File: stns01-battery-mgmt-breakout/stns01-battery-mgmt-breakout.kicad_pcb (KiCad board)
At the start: 2 copper layers, 0 parts

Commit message: Generate BOM. Initial parts placement.
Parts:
- added C1: 2.2uF, Wickerlib:RLC-0603-SMD, F.Cu at (62.5, 44.0)
- added C2: 4.7uF, Wickerlib:RLC-0603-SMD, F.Cu at (64.2, 55.1)
- added C3: 2.2uF, Wickerlib:RLC-0603-SMD, F.Cu at (72.6, 55.8)
- added C4: 2.2uF, Wickerlib:RLC-0603-SMD, F.Cu at (70.4, 55.8)
- added J1: MICRO USB, Wickerlib:CONN-USB-MICRO-B-AMPHENOL-10118193-0001LF, F.Cu at (56.5, 44.0)
- added J2: PH, Wickerlib:CONN-JST-S2B-PH-SM4-TB, F.Cu at (55.7, 55.1)
- added J3: POWER PINS, Wickerlib:CONN-HEADER-STRAIGHT-P2.54MM-1x07, F.Cu at (91.9, 47.4)
- added J4: CONTROL PINS, Wickerlib:CONN-HEADER-STRAIGHT-P2.54MM-1x07, F.Cu at (72.8, 74.7)
- added LED1: RED, Wickerlib:LED-0603-SMD, F.Cu at (76.5, 58.0)
- added R1: 0 ohm, Wickerlib:RLC-0603-SMD, F.Cu at (80.7, 53.6)
- added R2: 10K, Wickerlib:RLC-0603-SMD, F.Cu at (80.9, 56.1)
- added R3: NTC 10K, Wickerlib:RLC-0603-SMD, F.Cu at (80.8, 58.0)
- added R4: 604, Wickerlib:RLC-0603-SMD, F.Cu at (76.6, 61.1)
- added R5: 10K, Wickerlib:RLC-0603-SMD, F.Cu at (80.8, 54.5)
- added R6: 10K, Wickerlib:RLC-0603-SMD, F.Cu at (85.8, 55.4)
- added S1: SHUNT, Wickerlib:CONN-HEADER-STRAIGHT-P2.54MM-1x03, F.Cu at (82.2, 40.3)
- added S2: SLIDE, Wickerlib:SWITCH-ESWITCH-SLIDE-TH-EG1218, F.Cu at (100.1, 39.5)
- added U1: STNS01, Wickerlib:DFN-12-1EP-3x3MM-P0.45MM, F.Cu at (76.5, 54.5)
- added U2: LDO REG 3.3V, Wickerlib:SOT-23-3, F.Cu at (76.9, 48.1)
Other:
- rule trace_clearance: 0.1524 -> 0.254

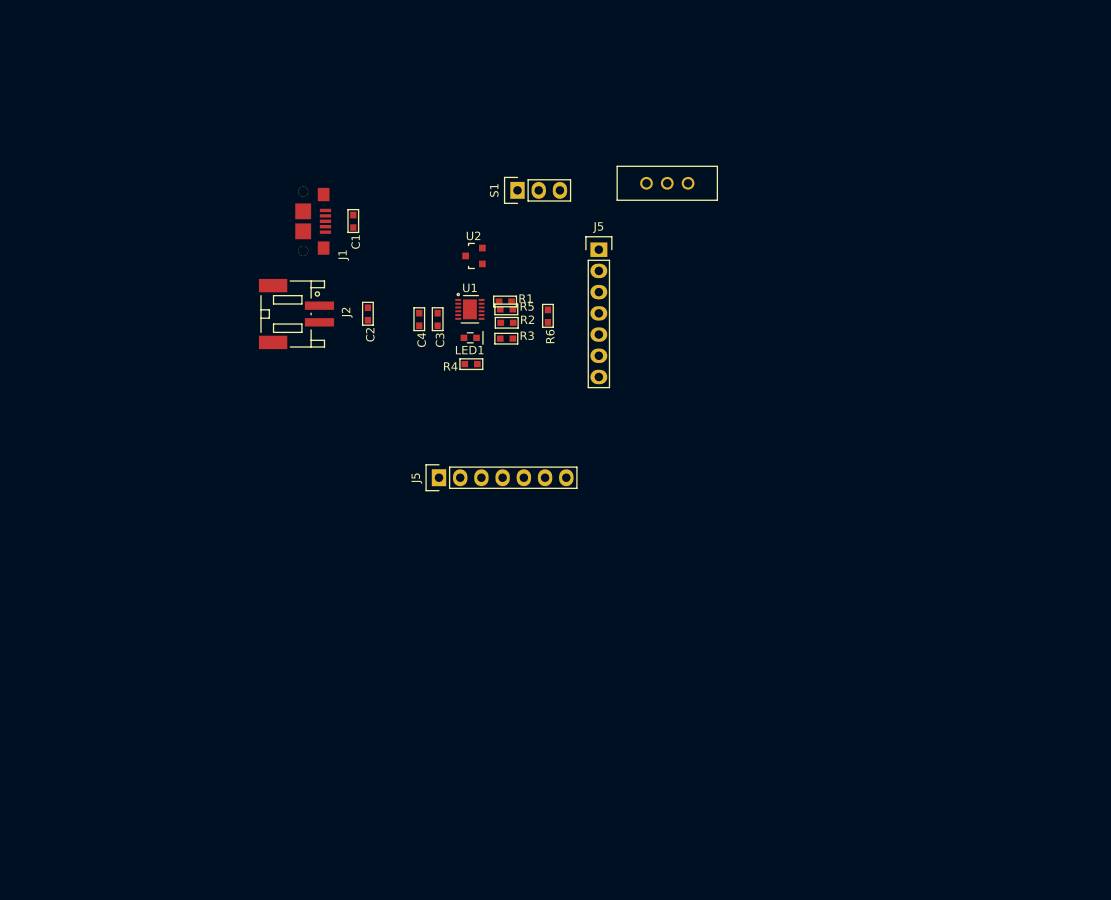
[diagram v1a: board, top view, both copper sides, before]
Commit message: Release v1.0 STNS01 battery breakout, needs tested.
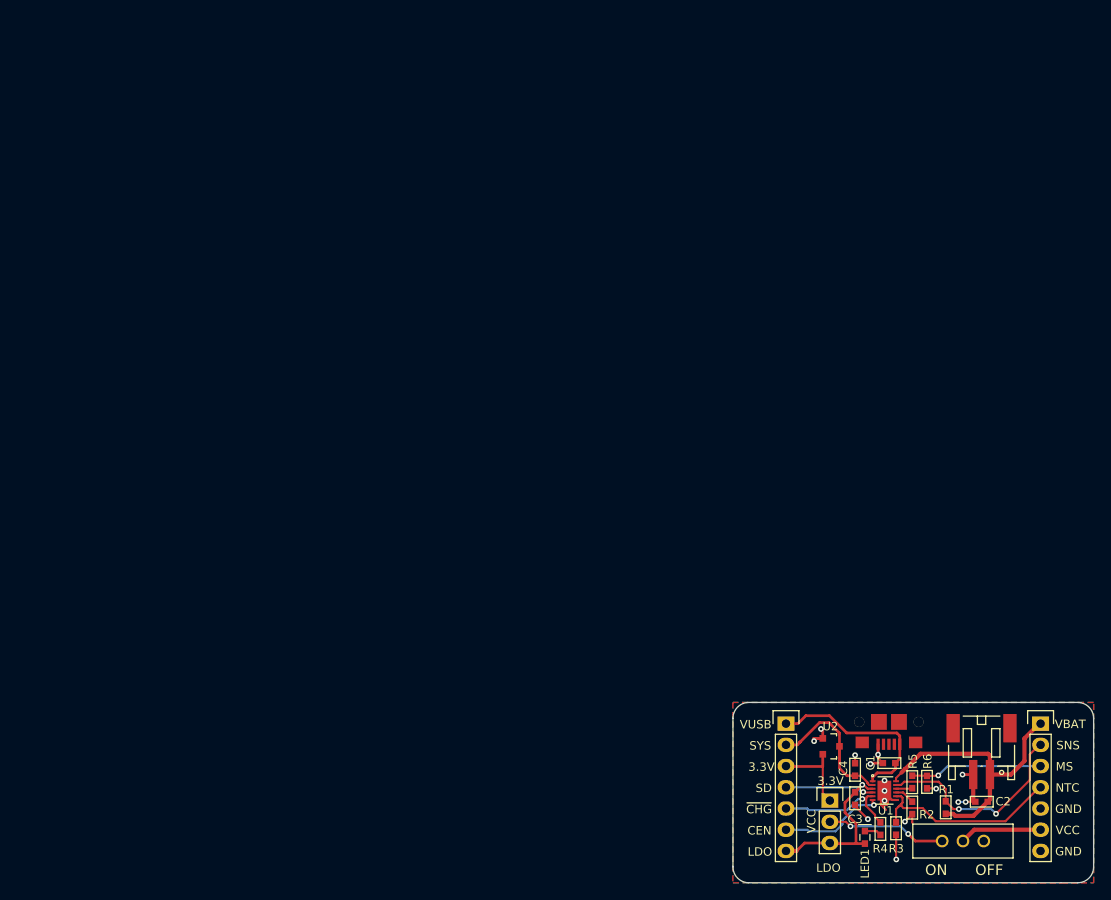
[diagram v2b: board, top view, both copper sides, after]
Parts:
- moved J2 97.3 mm to (137.7, 107.5), turned to 180 degrees
- moved C2 93.8 mm to (137.7, 113.5), turned to 180 degrees
- moved J1 92.2 mm to (126.6, 103.9), turned to 180 degrees
- moved C1 91.2 mm to (126.6, 108.9), turned to 180 degrees
- moved S2 86.3 mm to (135.5, 118.2)
- moved S1 82.1 mm to (119.6, 113.4), turned to 0 degrees
- moved R1 80.3 mm to (133.4, 114.2), turned to 270 degrees
- moved J4 77.8 mm to (144.8, 104.1), turned to 0 degrees
- moved LED1 76.2 mm to (123.7, 117.8), turned to 270 degrees
- moved C3 76.1 mm to (122.6, 113.1)
- moved U1 76.0 mm to (126.1, 112.2)
- moved R2 75.7 mm to (129.4, 114.2), turned to 270 degrees
- moved C4 75.0 mm to (122.6, 109.6), turned to 90 degrees
- moved R3 74.9 mm to (127.5, 116.7), turned to 270 degrees
- moved R5 74.6 mm to (129.4, 111.1), turned to 90 degrees
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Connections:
- net Net-(R2-Pad1) renamed /ISET
- C3 pad 1: /3.1V -> /LDO
- J3 pad 2: VBAT -> /SYS
- J3 pad 4: /3.1V -> /BAT_SD
- J3 pad 5: VCC -> /~BAT_CHG
- J3 pad 6: /SYS -> /BAT_CEN
- J3 pad 7: /3.1V -> /LDO
- J4 pad 1: VCC -> VBAT
- J4 pad 2: /~BAT_CHG -> /BATSNS
- J4 pad 4: /BAT_CEN -> /BAT_NTC
- J4 pad 5: /BAT_SD -> GND
- J4 pad 6: /BAT_NTC -> VCC
- LED1 pad 2: /3.1V -> /LDO
- R1 pad 1: Net-(R1-Pad1) -> /BATSNS
- S1 pad 3: /3.1V -> /LDO
- U1 pad 11: Net-(R1-Pad1) -> /BATSNS
- U1 pad 3: /3.1V -> /LDO
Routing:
- net GND: track 0.00 -> 40.8 mm, vias 0 -> 15
- net VBAT: track 0.00 -> 34.5 mm
- net /BATSNS: track 0.00 -> 25.1 mm, vias 0 -> 2
- net /BAT_NTC: track 0.00 -> 23.6 mm
- net VUSB: track 0.00 -> 22.8 mm
- net /LDO: track 0.00 -> 19.8 mm, vias 0 -> 1
- net /SYS: track 0.00 -> 19.6 mm
- net /BAT_MS: track 0.00 -> 15.9 mm, vias 0 -> 1
- net /~BAT_CHG: track 0.00 -> 14.8 mm, vias 0 -> 1
- net /TRANS: track 0.00 -> 14.4 mm, vias 0 -> 2
- net /BAT_CEN: track 0.00 -> 12.9 mm, vias 0 -> 1
- net /3.3V: track 0.00 -> 10.7 mm
- net /BAT_SD: track 0.00 -> 10.6 mm, vias 0 -> 1
- net VCC: track 0.00 -> 10.0 mm
- net /ISET: track 0.00 -> 2.39 mm
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- added copper zone on B.Cu, net GND
- added copper zone on F.Cu, net GND
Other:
- board outline added: 43.2 x 21.6 mm
- net class Default: clearance 0.254 -> 0.1524
- rule trace_clearance: 0.254 -> 0.1524
- board text added: "3.3V"
- board text added: "CEN"
- board text added: "GND"
- board text added: "LDO"
- board text added: "MS"
- board text added: "NTC"
- board text added: "ON OFF"
- board text added: "SD"
- board text added: "SNS"
- board text added: "STNS01 Battery Manager Breakout Board v1.0"
- board text added: "SYS"
- board text added: "VBAT"
- board text added: "VCC"
- board text added: "VUSB"
- board text added: "wickerbox.net"
- board text added: "~CHG"

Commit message: Updating v1.0 with FabNotes file.
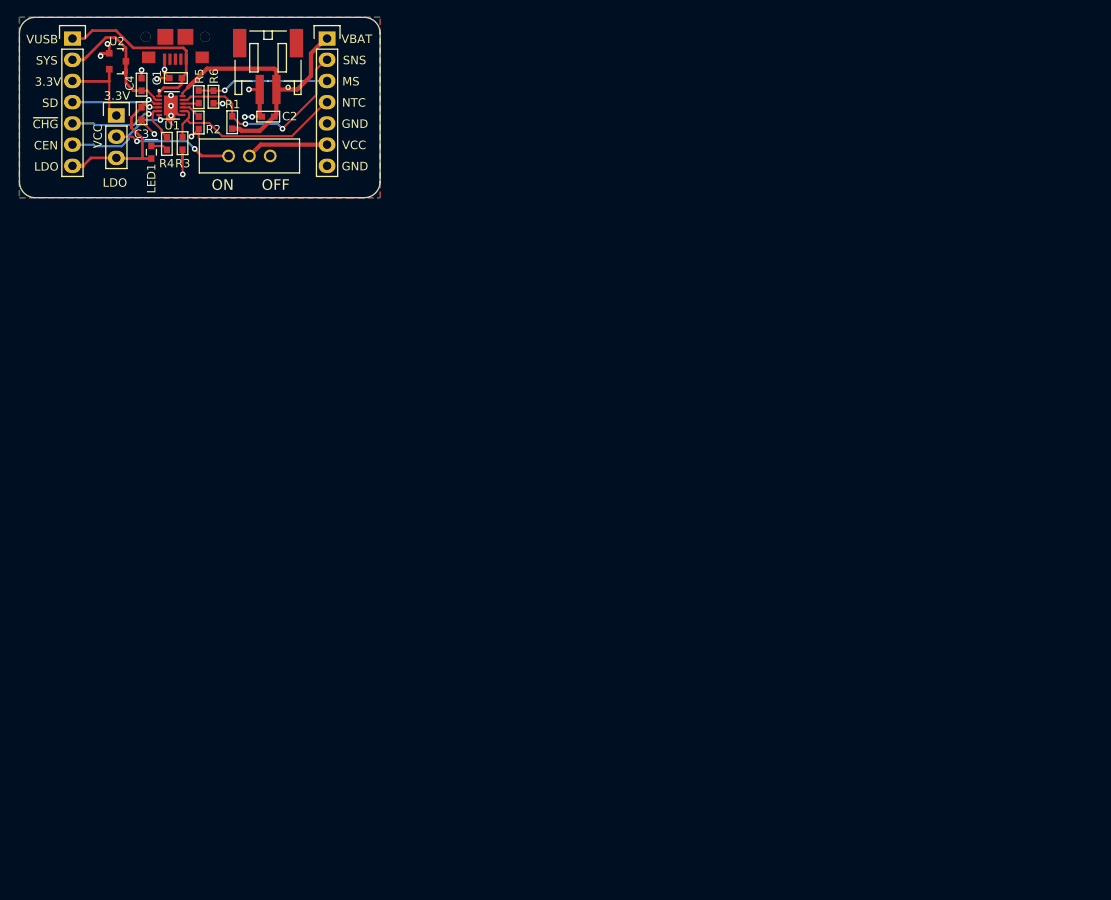
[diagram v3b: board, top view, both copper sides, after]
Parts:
- moved C1 118.4 mm to (41.2, 26.8)
- moved C4 118.4 mm to (37.2, 27.6)
- moved LED1 118.4 mm to (38.3, 35.7)
- moved R1 118.4 mm to (48.0, 32.2)
- moved R2 118.4 mm to (44.0, 32.2)
- moved R5 118.4 mm to (44.0, 29.1)
- moved S1 118.4 mm to (34.1, 31.3)
- moved S2 118.4 mm to (50.1, 36.2)
- moved C2 118.4 mm to (52.3, 31.5)
- moved C3 118.4 mm to (37.2, 31.1)
- moved J1 118.4 mm to (41.2, 21.9)
- moved J2 118.4 mm to (52.3, 25.4)
- moved J3 118.4 mm to (28.9, 22.1)
- moved J4 118.4 mm to (59.4, 22.1)
- moved R3 118.4 mm to (42.1, 34.7)
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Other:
- board text added: "FABRICATION NOTES 1. THIS IS A 2 LAYER BOARD. 2. EXTERNAL LAYERS SHALL HAVE 1 OZ COPPER. 3. MATERIAL: FR4 AND 0.062 INCH +/- 10% THICK. 4. BOARDS SHALL BE ROHS COMPLIANT. 5. MANUFACTURE IN ACCORDANCE WITH IPC-6012 CLASS 2 6. MASK: BOTH SIDES OF THE BOARD SHALL HAVE SOLDER MASK (ANY COLOR) OVER BARE COPPER. 7. SILK: BOTH SIDES OF THE BOARD SHALL HAVE WHITE SILKSCREEN. DO NOT PLACE SILK OVER BARE C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"
